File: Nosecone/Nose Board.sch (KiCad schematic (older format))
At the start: 1 part

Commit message: Couple little things before I give up for the night
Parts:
- added J1: Conn_01x02, symbol Conn_01x02
- added R1, R2: R, symbol R
- added U1: RS485_converter_ISL83488, symbol RS485_converter_ISL83488
- added U2: ATXMEGA16A4U-AU, TQFP44, symbol ATXMEGA16A4U-AU
- gave numbers to parts that had none: 1
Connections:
- new net +BATT: J1.1 (Pin_1), R1.1
- new net GND: J1.2 (Pin_2), R2.2
- new net Vbatt_meas: R1.2, R2.1, U2.40 (AREFA/AC0/ADC0/PA0)
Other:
- note added: "Battery connection"
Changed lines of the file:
@@
 $EndDescr
 $Comp
-L 3.3V_DCDC_Conv_TPS62056DGS U?
+L 3.3V_DCDC_Conv_TPS62056DGS U3
 U 1 1 5A373369
 P 5300 2050
-F 0 "U?" H 6300 1750 60  0000 C CNN
+F 0 "U3" H 6300 1750 60  0000 C CNN
 F 1 "3.3V_DCDC_Conv_TPS62056DGS" H 6350 1950 60  0000 C CNN
 F 2 "" H 5300 2050 60  0001 C CNN
@@
 	1    0    0    -1
 $EndComp
+$Comp
+L RS485_converter_ISL83488 U1
+U 1 1 5A373694
+P 2900 1050
+F 0 "U1" H 3850 800 60  0000 C CNN
+F 1 "RS485_converter_ISL83488" H 3850 250 60  0000 C CNN
+F 2 "" H 2900 1050 60  0001 C CNN
+F 3 "" H 2900 1050 60  0001 C CNN
+	1    2900 1050
+	1    0    0    -1
+$EndComp
+$Comp
+L ATXMEGA16A4U-AU U2
+U 1 1 5A3736DB
+P 3550 3600
+F 0 "U2" H 2800 4800 50  0000 L BNN
+F 1 "ATXMEGA16A4U-AU" H 3900 2350 50  0000 L BNN
+F 2 "TQFP44" H 3550 3600 50  0001 C CIN
+F 3 "" H 3550 3600 50  0001 C CNN
+	1    3550 3600
+	1    0    0    -1
+$EndComp
+$Comp
+L Conn_01x02 J1
+U 1 1 5A373718
+P 8700 1300
+F 0 "J1" H 8700 1400 50  0000 C CNN
+F 1 "Conn_01x02" H 8700 1100 50  0000 C CNN
+F 2 "" H 8700 1300 50  0001 C CNN
+F 3 "" H 8700 1300 50  0001 C CNN
+	1    8700 1300
+	1    0    0    -1
+$EndComp
+$Comp
+L +BATT #PWR1
+U 1 1 5A373765
+P 8350 950
+F 0 "#PWR1" H 8350 800 50  0001 C CNN
+F 1 "+BATT" H 8350 1090 50  0000 C CNN
+F 2 "" H 8350 950 50  0001 C CNN
+F 3 "" H 8350 950 50  0001 C CNN
+	1    8350 950
+	1    0    0    -1
+$EndComp
+Wire Wire Line
+	8350 950  8350 1300
+Wire Wire Line
+	8350 1300 8500 1300
+$Comp
+L GND #PWR2
+U 1 1 5A3737AD
+P 8350 1900
+F 0 "#PWR2" H 8350 1650 50  0001 C CNN
+F 1 "GND" H 8350 1750 50  0000 C CNN
+F 2 "" H 8350 1900 50  0001 C CNN
+F 3 "" H 8350 1900 50  0001 C CNN
+	1    8350 1900
+	1    0    0    -1
+$EndComp
+Wire Wire Line
+	8350 1400 8350 1900
+Wire Wire Line
+	8350 1400 8500 1400
+$Comp
+L R R1
+U 1 1 5A3737D1
+P 7850 1250
+F 0 "R1" V 7930 1250 50  0000 C CNN
+F 1 "R" V 7850 1250 50  0000 C CNN
+F 2 "" V 7780 1250 50  0001 C CNN
+F 3 "" H 7850 1250 50  0001 C CNN
+	1    7850 1250
+	1    0    0    -1
+$EndComp
+$Comp
+L R R2
+U 1 1 5A373800
+P 7850 1650
+F 0 "R2" V 7930 1650 50  0000 C CNN
+F 1 "R" V 7850 1650 50  0000 C CNN
+F 2 "" V 7780 1650 50  0001 C CNN
+F 3 "" H 7850 1650 50  0001 C CNN
+	1    7850 1650
+	1    0    0    -1
+$EndComp
+Wire Wire Line
+	7850 1100 8350 1100
+Connection ~ 8350 1100
+Wire Wire Line
+	7850 1400 7850 1500
+Wire Wire Line
+	7850 1800 7850 1850
+Wire Wire Line
+	7850 1850 8350 1850
+Connection ~ 8350 1850
+Wire Notes Line
+	7600 750  7600 2150
+Wire Notes Line
+	7600 2150 9000 2150
+Wire Notes Line
+	9000 2150 9000 700
+Wire Notes Line
+	9000 700  7600 700
+Wire Notes Line
+	7600 700  7600 800
+Text Notes 7900 650  0    60   ~ 0
+Battery connection
+Text Label 7850 1450 0    60   ~ 0
+Vbatt_meas
+Text Label 4450 2600 0    60   ~ 0
+Vbatt_meas
 $EndSCHEMATC

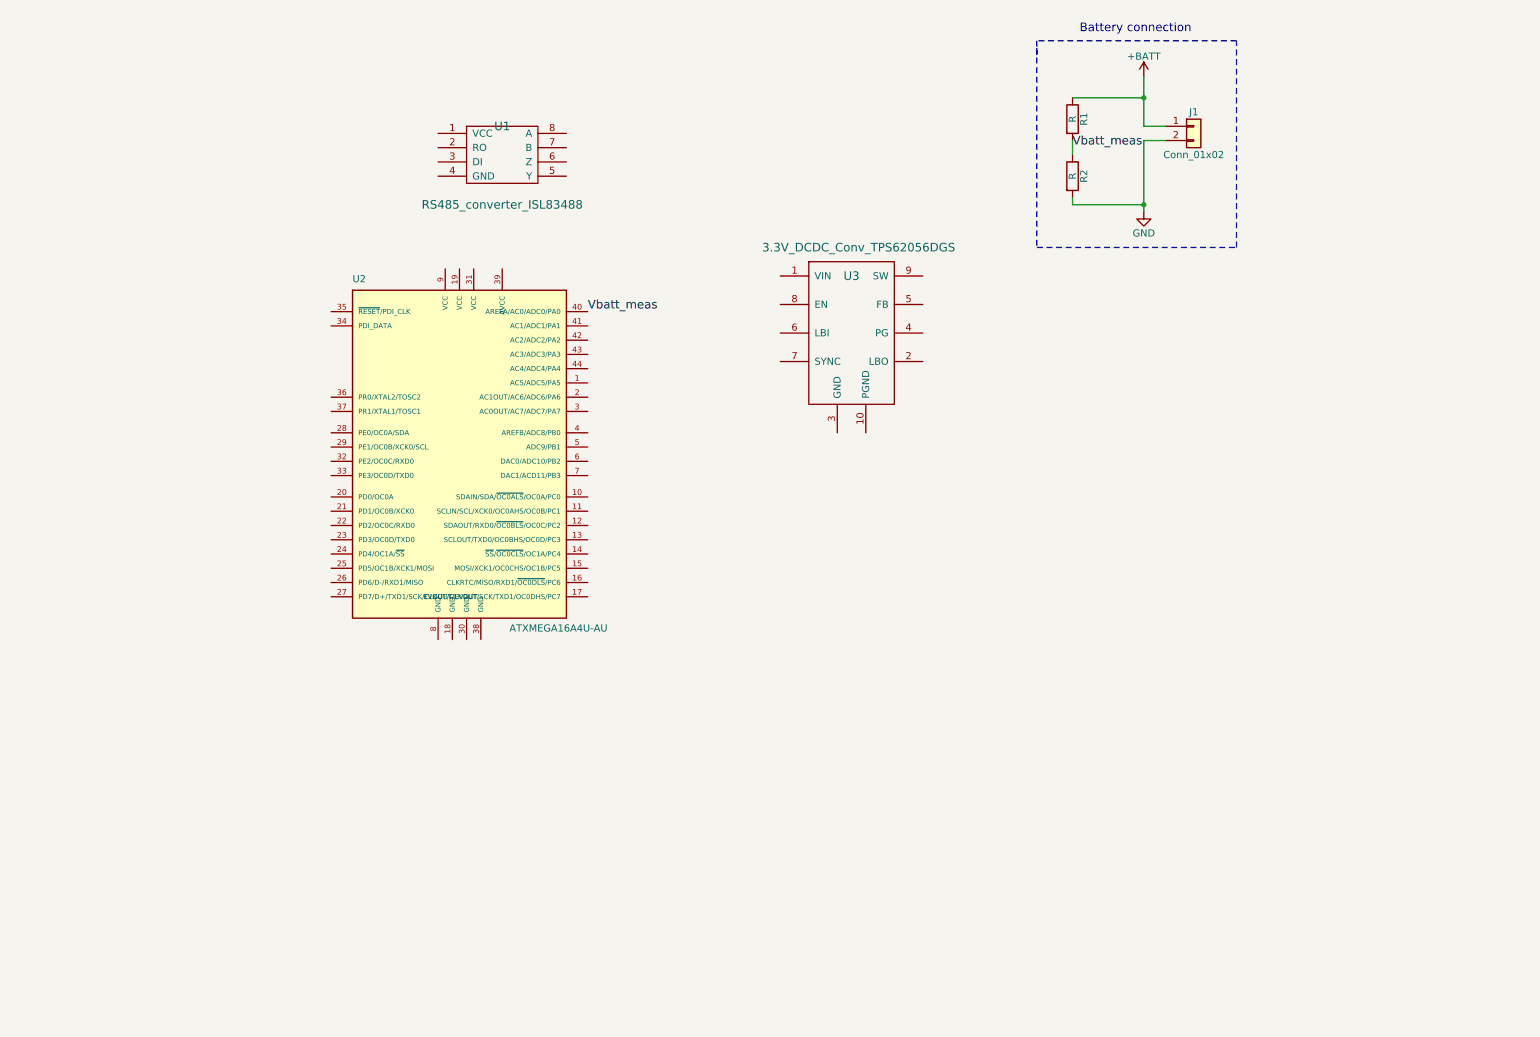
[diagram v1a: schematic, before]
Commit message: Added components, some nets
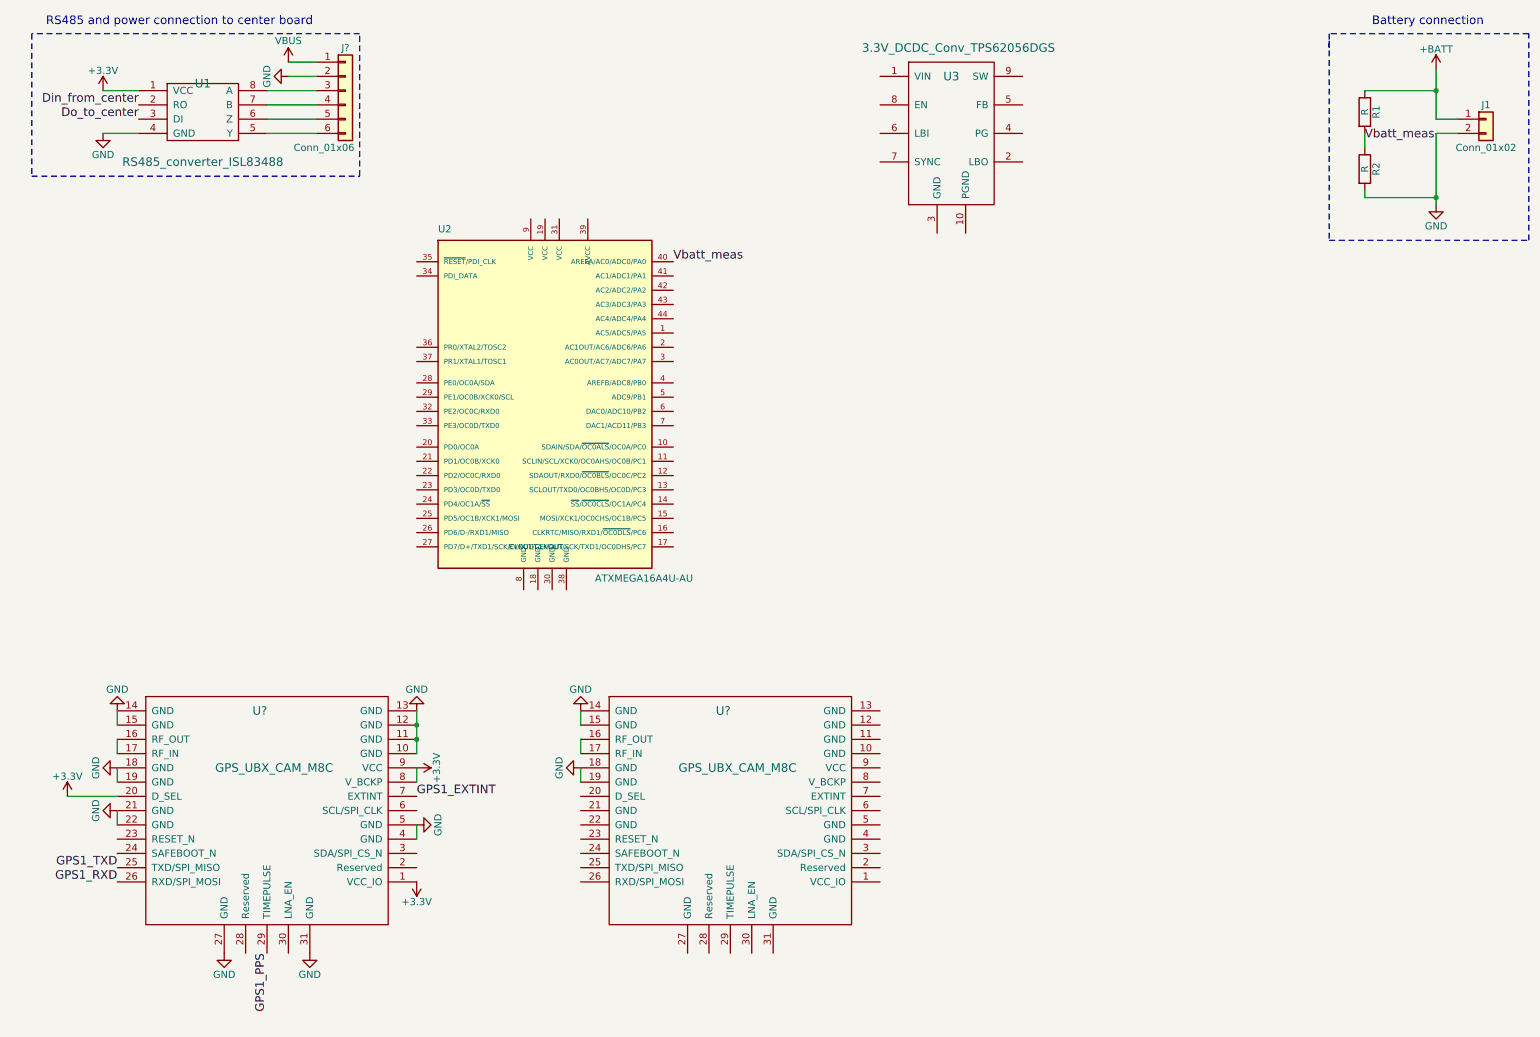
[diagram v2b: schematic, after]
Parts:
- added J?: Conn_01x06, symbol Conn_01x06
- added U? (x2): GPS_UBX_CAM_M8C, symbol GPS_UBX_CAM_M8C
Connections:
- net GND: now also U1.4 (GND), J?.2 (Pin_2), U?.10 (GND), U?.11 (GND), U?.12 (GND), U?.13 (GND), U?.14 (GND), U?.14 (GND), U?.15 (GND), U?.15 (GND), U?.18 (GND), U?.18 (GND), U?.19 (GND), U?.19 (GND), U?.21 (GND), U?.22 (GND), U?.27 (GND), U?.31 (GND), U?.4 (GND), U?.5 (GND)
- net +3V3: now reaches U1.1 (VCC)
- net +3V3: now also U?.1 (VCC_IO), U?.20 (D_SEL), U?.8 (V_BCKP), U?.9 (VCC)
- net Din_from_center: now reaches U1.2 (RO)
- net Do_to_center: now reaches U1.3 (DI)
- net at U1.5 (Y): now also J?.6 (Pin_6)
- net at U1.6 (Z): now also J?.5 (Pin_5)
- net at U1.7 (B): now also J?.4 (Pin_4)
- net at U1.8 (A): now also J?.3 (Pin_3)
- new net: U?.16 (RF_OUT), U?.17 (RF_IN) (x2)
- new net GPS1_EXTINT: U?.7 (EXTINT)
- new net GPS1_PPS: U?.29 (TIMEPULSE)
- new net GPS1_RXD: U?.26 (RXD/SPI_MOSI)
- new net GPS1_TXD: U?.25 (TXD/SPI_MISO)
- new net VBUS: J?.1 (Pin_1)
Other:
- note added: "RS485 and power connection to center board"
- moved on the sheet: J1, R1, R2, U1, U2, U3

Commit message: Added more components to schematic
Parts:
- added J?: Conn_02x03_Counter_Clockwise, Pin_Headers:Pin_Header_Straight_2x03_Pitch1.27mm, symbol Conn_02x03_Counter_Clockwise
- added U6: XBEE, RF:XBEE, symbol XBEE
- J1: footprint (none) -> Pin_Headers:Pin_Header_Straight_1x02_Pitch1.27mm
- J2: renamed from J?; footprint (none) -> Pin_Headers:Pin_Header_Straight_1x06_Pitch1.27mm
- R1, R2: footprint (none) -> Resistors_SMD:R_0603_HandSoldering
- U1: footprint (none) -> Misc components:SOIC-8
- U2: footprint TQFP44 -> Misc components:QFP_44
- U3: footprint (none) -> Misc components:SOIC-10
- U4, U5: renamed from U?; footprint (none) -> Misc components:UBX_CAM-M8C
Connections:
- net labels added: GPS2_EXTINT, GPS2_PPS, GPS2_RXD, GPS2_TXD
- wire segments 27 -> 32

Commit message: Started inserting smaller circuit components
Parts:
- added C? (x4): C, symbol C
- added C?: 10uF, symbol C
- added C?: 22uF, symbol C
- added L?: 10uH, symbol L
- added Q? (x2): Q_PMOS_DGS, symbol Q_PMOS_DGS
- added R?: 470k, symbol R
- added R? (x2): R, symbol R
- added R? (x2): 1M, symbol R
- added U7: OpenLog, Pin_Headers:Pin_Header_Straight_1x06_Pitch2.54mm, symbol OpenLog
- added U?: LTC4412, Misc components:SOIC-6, symbol LTC4412
- gave numbers to parts that had none: 1
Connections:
- net labels added: VDC
- wire segments 32 -> 72
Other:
- note added: "Power supply selection"
- moved on the sheet: U3

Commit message: Schematic complete, pending review
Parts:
- removed J3: Conn_02x03_Counter_Clockwise, Pin_Headers:Pin_Header_Straight_2x03_Pitch1.27mm, symbol Conn_02x03_Counter_Clockwise
- added C?: 10uF, symbol C
- added C?: 100nF, symbol C
- added D? (x2): LED, symbol LED
- added FB?: FERRITE_BEAD-0603, 0603, symbol FERRITE_BEAD-0603
- added J?: Conn_02x03_Odd_Even, symbol Conn_02x03_Odd_Even
- added J?: Conn_01x04, symbol Conn_01x04
- added R?: 10k, symbol R
- added U?: BNO055, symbol BNO055
- R?: value R -> 130k
- R?: value R -> 100k
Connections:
- net labels added: Center_Din, Center_Dout, IMU_INT, IMU_SCL, IMU_SDA, LED_STATUS1, LED_STATUS2, PDI_CLK, PDI_Data, XBEE_Din, XBEE_Dout, XBee_Din
- net labels removed: Din_from_center, Do_to_center
- wire segments 72 -> 88
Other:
- note added: "3.3V Converter"
- note added: "GPSes (GPSi?)"
- note added: "IMU"
- note added: "OpenLog"
- note added: "Programming Port"
- note added: "Serial Debug Connection"
- note added: "Status LEDs"
- note added: "VBUS - power from center board (>3.3V)\n+BATT - battery power (>3.3V)\nVDC - selected power line (>3.3V)\n+3.3V - converter output"
- note added: "XBee"
- moved on the sheet: C?, L?, R?, U3, U6, U7

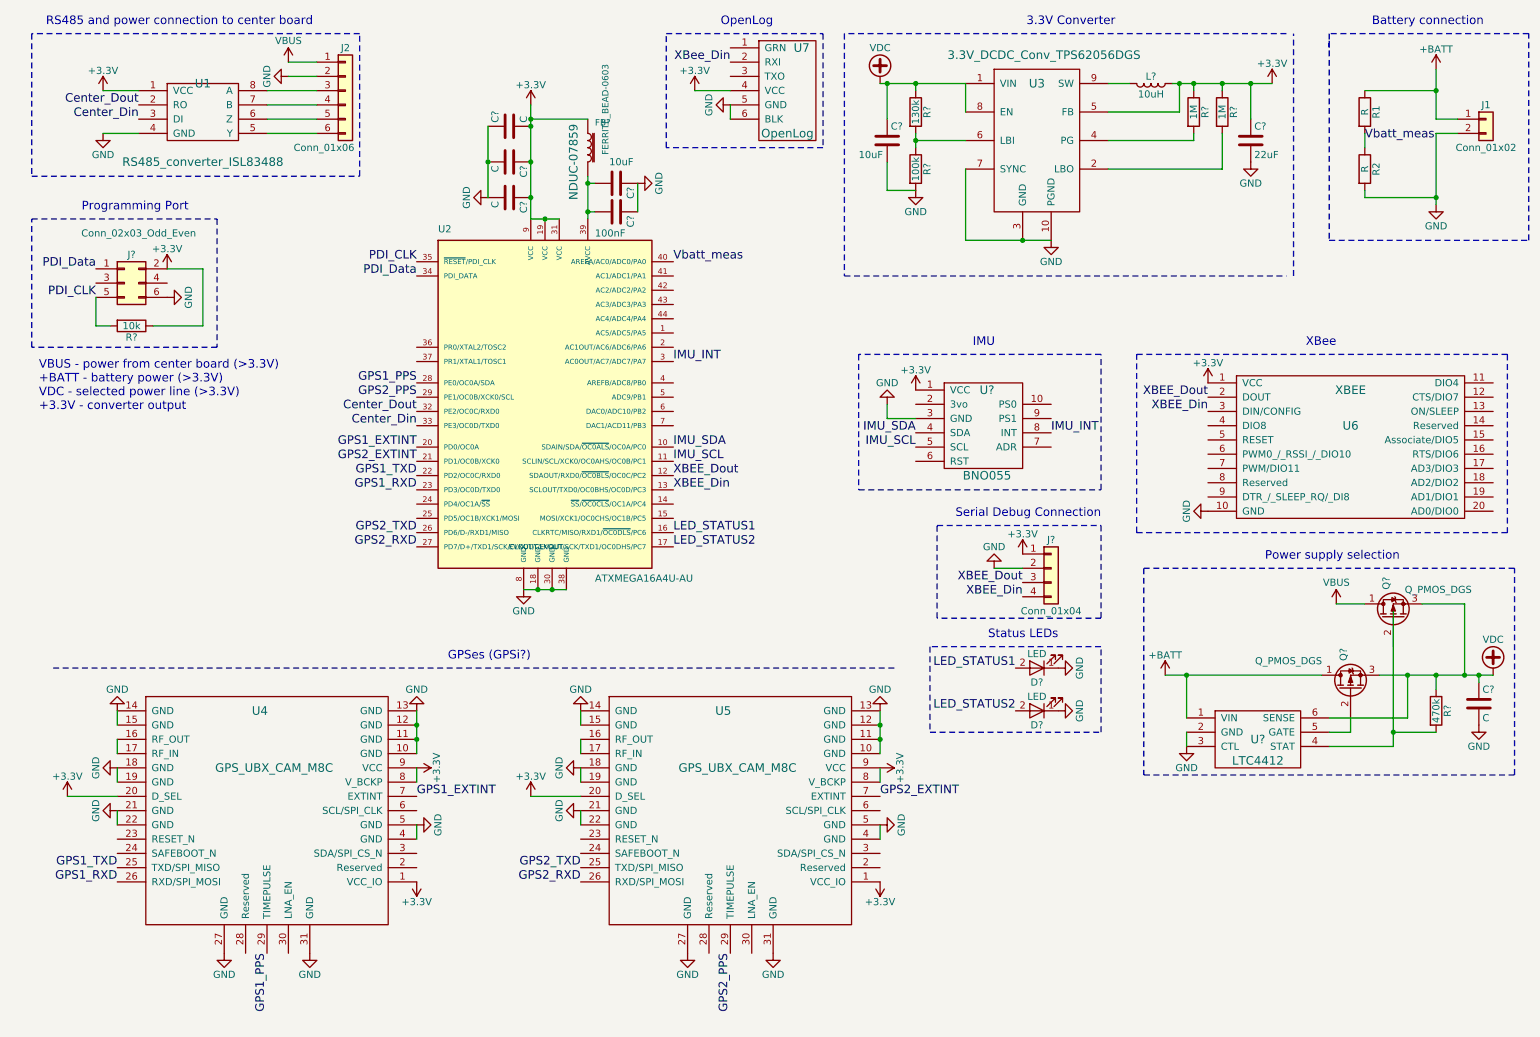
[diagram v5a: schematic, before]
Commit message: Added pressure sensors, began routing
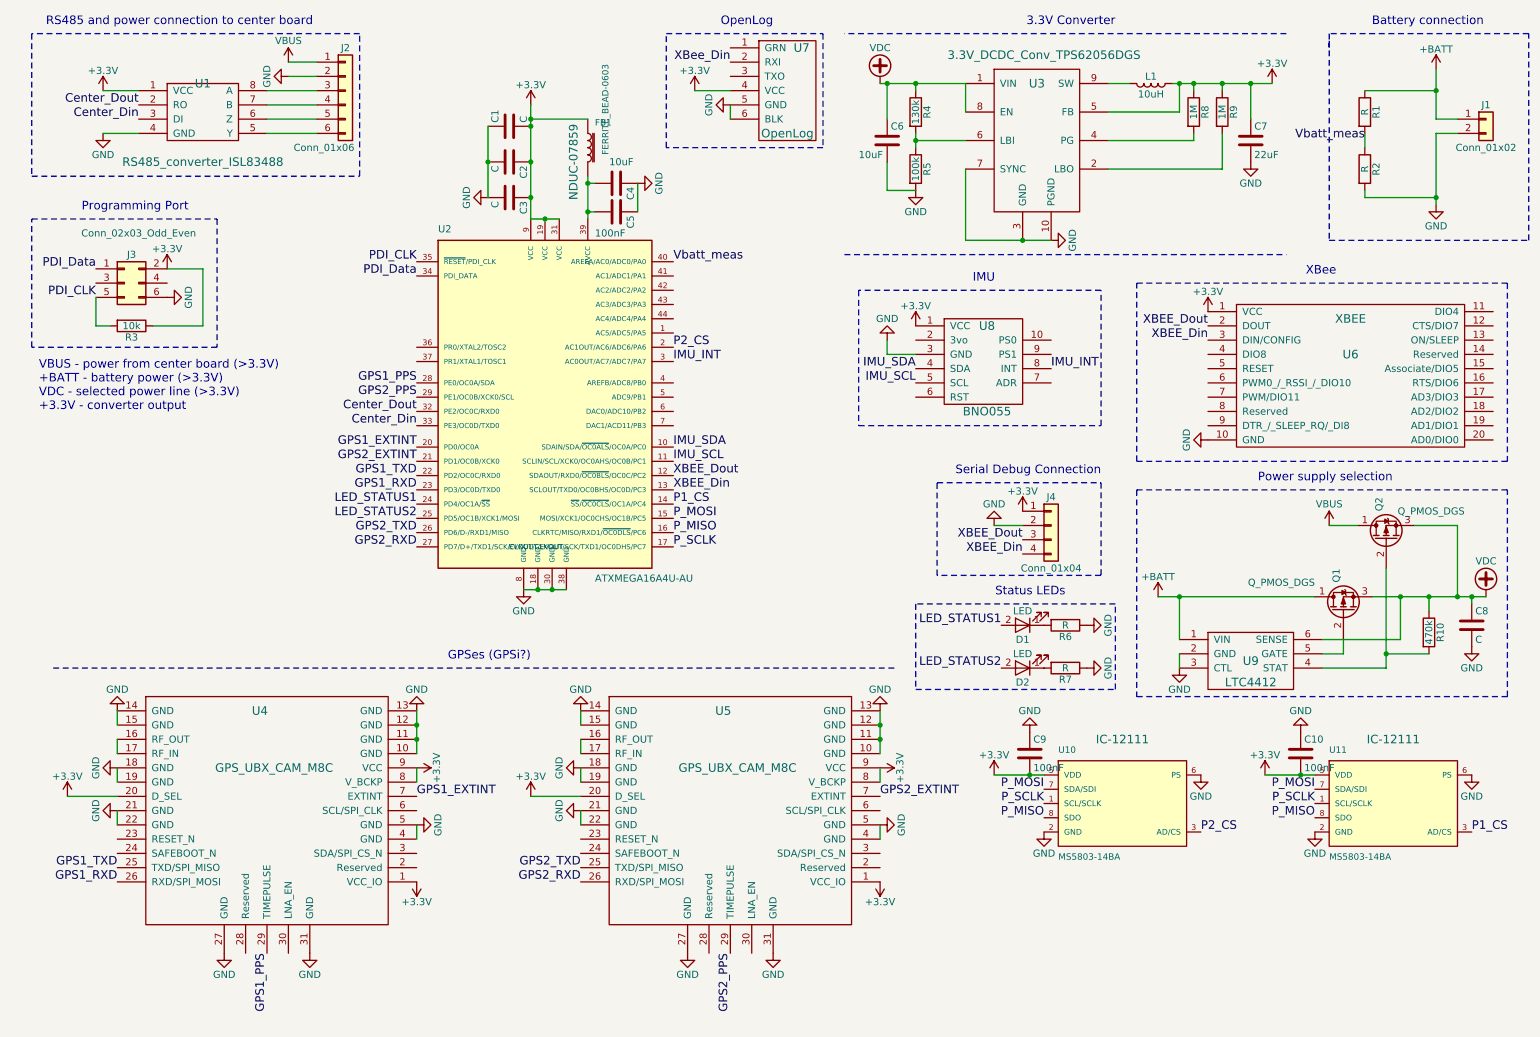
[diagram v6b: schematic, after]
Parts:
- added C10, C9: 100nF, Capacitors_SMD:C_0603_HandSoldering, symbol C
- added R6, R7: R, Resistors_SMD:R_0603_HandSoldering, symbol R
- added U10, U11: MS5803-14BA, Silicon-Standard:MS5803, symbol MS5803-14BA
- C1, C2, C3, C4, C5, C6, C7, C8: renamed from C?; footprint (none) -> Capacitors_SMD:C_0603_HandSoldering
- D1, D2: renamed from D?; footprint (none) -> LEDs:LED_0603_HandSoldering
- FB1: renamed from FB?; footprint 0603 -> Inductors_SMD:L_0603_HandSoldering
- J3: renamed from J?; footprint (none) -> Pin_Headers:Pin_Header_Straight_2x03_Pitch1.27mm
- J4: renamed from J?; footprint (none) -> Pin_Headers:Pin_Header_Straight_1x04_Pitch1.27mm
- L1: renamed from L?; footprint (none) -> Inductors_SMD:L_7.3x7.3_H4.5
- Q1, Q2: renamed from Q?; footprint (none) -> TO_SOT_Packages_SMD:SOT-223-3_TabPin2
- R10, R3, R4, R5, R8, R9: renamed from R?; footprint (none) -> Resistors_SMD:R_0603_HandSoldering
- U8: renamed from U?; footprint (none) -> Misc components:BNO055_Breakout
- gave numbers to parts that had none: 1
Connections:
- net +3V3: now also C10.2, C9.2, U10.5 (VDD), U11.5 (VDD)
- net GND: now also C10.1, C9.1, R6.1, R7.1, U10.2 (GND), U10.6 (PS), U11.2 (GND), U11.6 (PS); no longer D1.1 (K), D2.1 (K)
- net LED_STATUS1: now also U2.24 (PD4/OC1A/~SS~); no longer U2.16 (CLKRTC/MISO/RXD1/~OC0DLS~/PC6)
- net LED_STATUS2: now also U2.25 (PD5/OC1B/XCK1/MOSI); no longer U2.17 (EVOUT/CLKOUT/SCK/TXD1/OC0DHS/PC7)
- net P1_CS: now reaches U2.14 (~SS~/~OC0CLS~/OC1A/PC4)
- net P1_CS: now also U11.3 (AD/CS)
- net P_MOSI: now reaches U2.15 (MOSI/XCK1/OC0CHS/OC1B/PC5)
- net P_MOSI: now also U10.7 (SDA/SDI), U11.7 (SDA/SDI)
- net P2_CS: now reaches U2.2 (AC1OUT/AC6/ADC6/PA6)
- net P2_CS: now also U10.3 (AD/CS)
- net at R10.2, U9.4 (STAT): now also Q2.2 (G)
- new net: D2.1 (K), R7.2
- new net: D1.1 (K), R6.2
- new net P_MISO: U10.8 (SDO), U11.8 (SDO), U2.16 (CLKRTC/MISO/RXD1/~OC0DLS~/PC6)
- new net P_SCLK: U10.1 (SCL/SCLK), U11.1 (SCL/SCLK), U2.17 (EVOUT/CLKOUT/SCK/TXD1/OC0DHS/PC7)
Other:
- moved on the sheet: C8, D1, D2, J4, Q1, Q2, R10, U6, U8, U9
